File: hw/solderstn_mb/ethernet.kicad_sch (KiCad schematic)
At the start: 36 parts, among them J201 74980104400, U201 IP101GA, U202 74LVC1G126SE, Y201 TSX-3225 25.0000MF10P-C

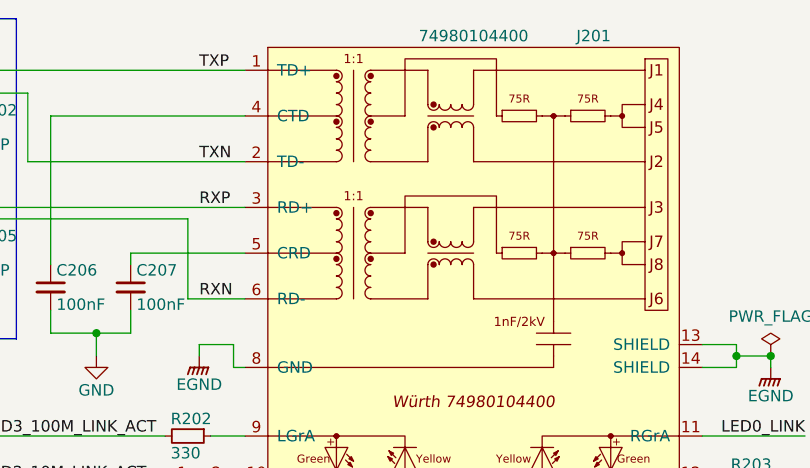
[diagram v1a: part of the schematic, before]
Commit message: hw: long-standing uncommitted stuff; mostly auto-updates (v7) fw: remove L052 tree (CMSIS & std-HAL shouldn't be committed and it was the wrong device name anyway)
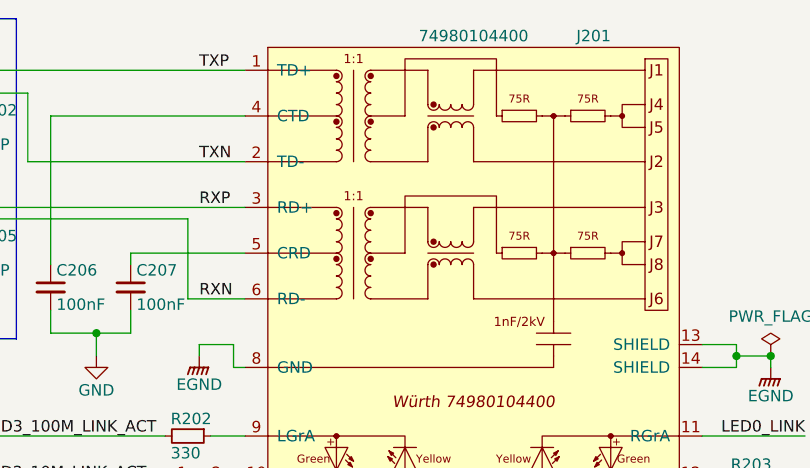
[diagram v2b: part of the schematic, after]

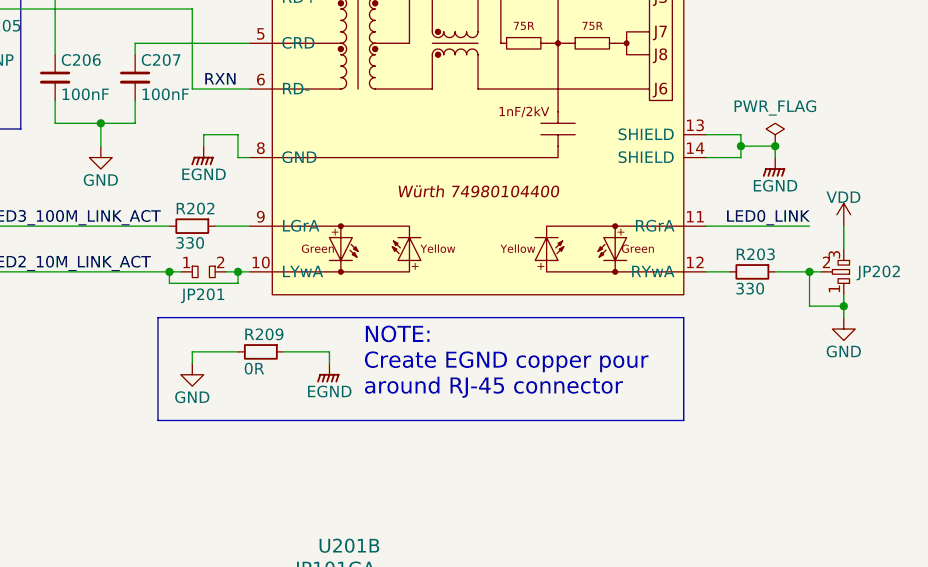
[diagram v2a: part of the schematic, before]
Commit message: Various boards & schematics (auto-)updated to Kicad-v8
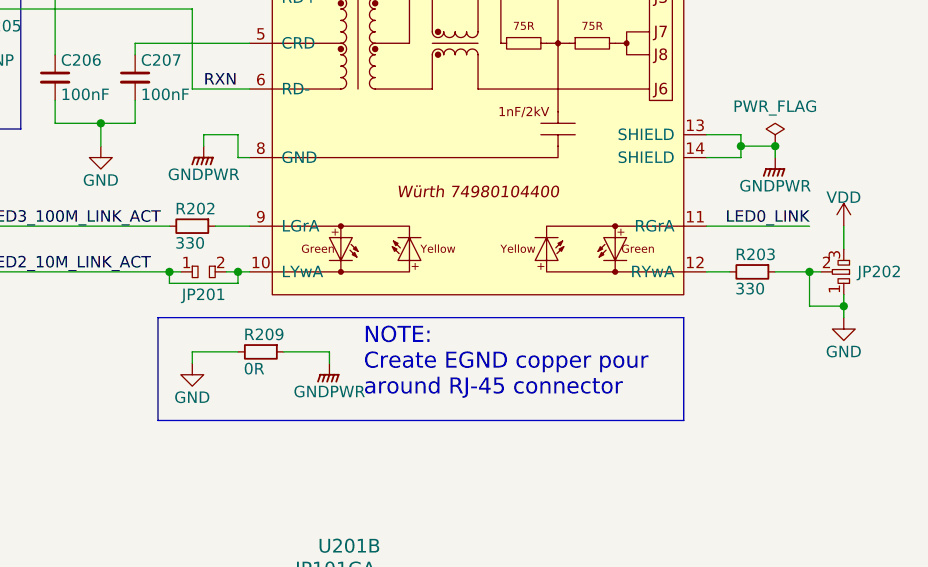
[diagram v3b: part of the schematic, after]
